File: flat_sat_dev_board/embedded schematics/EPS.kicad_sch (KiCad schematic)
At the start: 193 parts, among them IC3 PCT2075DP,118, IC4 LT3652IMSE#PBF, IC5 RP2040_QFN56, J12 Foot0, J13 Bypass, J14 ISS Foot, J15 Foot1, J16 Heater, J17 Foot2, J18 Barrel_Jack_Switch, J19 BURN, J20 Foot3, J21 CHARGE, J22 RBF, J24 BM04B-SRSS-TB(LF)(SN), J25 Life Makes Lemonade, J26 Jetson, J27 BM04B-SRSS-TB(LF)(SN), J28 BM04B-SRSS-TB(LF)(SN), J29 CHARGE, J30 CAN1, J31 I2C Multiplexer Breakout, J32 I2C0 Breakout, J34 Screw_Terminal_01x02, J35 Conn_ARM_JTAG_SWD_10, J36 USB_B_Micro, K1 APAN3109, Q10 NDS8434, Q11 MBT2222ADW1T1, Q12 MBT2222ADW1T1, Q2 MMBT2222AT, Q3 IRLML2803, Q4 IRLML2803, Q5 NDS8434, Q6 NDS8434, Q7 IRF7458, Q8 IRF7458, Q9 IRLML2803, SW3 KMR2, SW4 KMR2, U13 1049, U14 R5460N208AA, U15 1049, U16 TPS54226PWPRPWP14_2P31X2P46-L, U17 AD8495, U18 TLVH431 DBZ SOT-23, U19 INA219AxD, U20 INA219AxD, U21 MAX706RESA, U22 ADS1015IDGS, U23 W25Q128JV, U24 MCP25625-E/ML, U25 TPS54226PWPRPWP14_2P31X2P46-L, Y4 Crystal_GND24, Y5 Crystal_GND24

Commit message: Updated all the Diodes!
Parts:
- D10, D12, D7, D9: symbol mainboard:DFLS130L -> Device:D_Schottky
- D11, D6, D8: value D_Schottky -> DFLS130L; footprint Diode_SMD:D_SMB -> Diode_SMD:D_PowerDI-123
- J29: value CHARGE -> Solar Input
- J31: value I2C Multiplexer Breakout -> I2C0 Breakout
- J32: value I2C0 Breakout -> I2C1 Breakout
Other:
- note added: "Charging Threshold: ~8.3V Charge Cutoff: ~8.36V"
- moved on the sheet: C46, C47, C48, D11, D6, D8, IC4, J14, J18, J24, J25, J26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

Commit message: Updated Camera Board V2 with Production Files
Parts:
- removed R34: 200k, Resistor_SMD:R_0603_1608Metric, symbol mainboard:R-US_R0603
- added R1034, R1035: 100K, Resistor_SMD:R_0603_1608Metric, symbol Device:R_US
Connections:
- net at C46.1, D6.1 (K), D8.1 (K)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: now also R1034.1
- net at IC4.2 (VIN_REG), R35.2: now also R1035.2
- new net: R1034.2, R1035.1
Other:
- moved on the sheet: R35

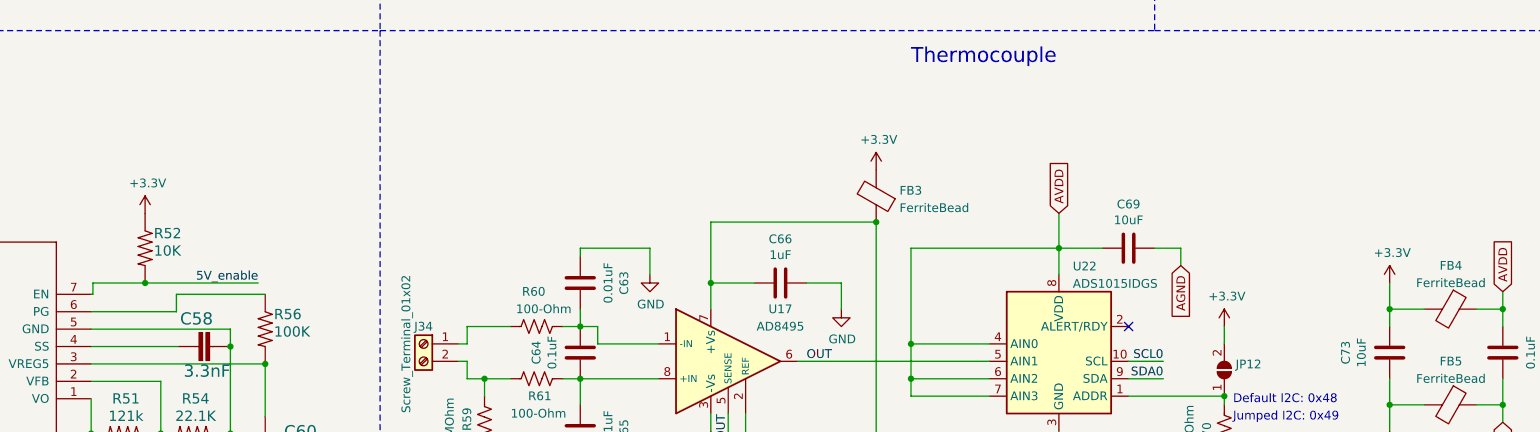
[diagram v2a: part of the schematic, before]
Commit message: Fixed References From 3.3V to be all 3V3
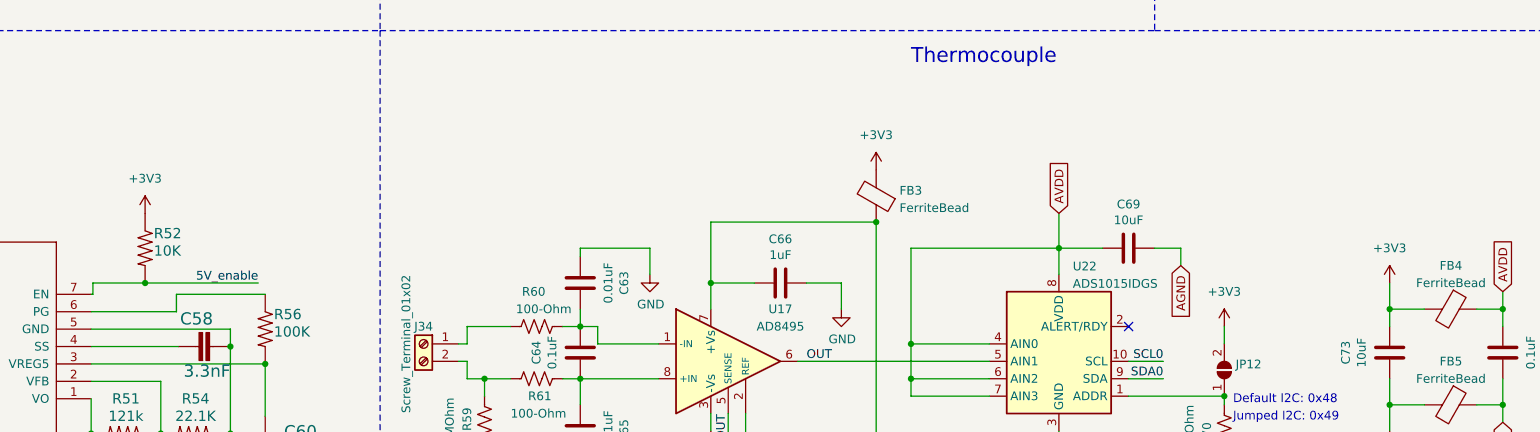
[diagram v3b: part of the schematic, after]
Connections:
- net +3.3V is gone; now on net +3V3: C73.2, FB3.2, FB4.2, JP12.2 (B), R52.1
